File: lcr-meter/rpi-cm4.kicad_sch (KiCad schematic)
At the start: 0 parts

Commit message: Added CM4, basics of functionality started
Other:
- added sheet GPIO (CM4_GPIO.kicad_sch)
- added sheet High-Speed (CM4_HighSpeed.kicad_sch)
- added sheet RTC (RTC.kicad_sch)
- added sheet USB Hub (USB2-HUB.kicad_sch)
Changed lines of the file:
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@@
 	(generator_version "8.0")
 	(paper "A4")
+	(sheet
+		(at 66.04 124.46)
+		(size 43.18 33.02)
+		(fields_autoplaced yes)
+		(stroke
+			(width 0.1524)
+			(type solid)
+		)
+		(fill
+			(color 0 0 0 0.0000)
+		)
+		(property "Sheetname" "RTC"
+			(at 66.04 123.7484 0)
+			(effects
+				(font
+					(size 1.27 1.27)
+				)
+				(justify left bottom)
+			)
+		)
+		(property "Sheetfile" "RTC.kicad_sch"
+			(at 66.04 158.0646 0)
+			(effects
+				(font
+					(size 1.27 1.27)
+				)
+				(justify left top)
+			)
+		)
+		(instances
+			(project "lcr-meter"
+				(path "/ba333b18-b098-477b-9dd4-aab7b9764d9c/fa0205ff-d840-4c89-b6d9-0bee6ad4a2ef"
+					(page "10")
+				)
+			)
+		)
+	)
+	(sheet
+		(at 77.47 55.88)
+		(size 33.02 25.4)
+		(fields_autoplaced yes)
+		(stroke
+			(width 0.1524)
+			(type solid)
+		)
+		(fill
+			(color 0 0 0 0.0000)
+		)
+		(property "Sheetname" "GPIO"
+			(at 77.47 55.1684 0)
+			(effects
+				(font
+					(size 1.27 1.27)
+				)
+				(justify left bottom)
+			)
+		)
+		(property "Sheetfile" "CM4_GPIO.kicad_sch"
+			(at 77.47 81.8646 0)
+			(effects
+				(font
+					(size 1.27 1.27)
+				)
+				(justify left top)
+			)
+		)
+		(instances
+			(project "lcr-meter"
+				(path "/ba333b18-b098-477b-9dd4-aab7b9764d9c/fa0205ff-d840-4c89-b6d9-0bee6ad4a2ef"
+					(page "9")
+				)
+			)
+		)
+	)
+	(sheet
+		(at 205.74 76.2)
+		(size 30.48 20.32)
+		(fields_autoplaced yes)
+		(stroke
+			(width 0.1524)
+			(type solid)
+		)
+		(fill
+			(color 0 0 0 0.0000)
+		)
+		(property "Sheetname" "USB Hub"
+			(at 205.74 75.4884 0)
+			(effects
+				(font
+					(size 1.27 1.27)
+				)
+				(justify left bottom)
+			)
+		)
+		(property "Sheetfile" "USB2-HUB.kicad_sch"
+			(at 205.74 97.1046 0)
+			(effects
+				(font
+					(size 1.27 1.27)
+				)
+				(justify left top)
+			)
+		)
+		(instances
+			(project "lcr-meter"
+				(path "/ba333b18-b098-477b-9dd4-aab7b9764d9c/fa0205ff-d840-4c89-b6d9-0bee6ad4a2ef"
+					(page "11")
+				)
+			)
+		)
+	)
+	(sheet
+		(at 132.08 55.88)
+		(size 40.64 66.04)
+		(fields_autoplaced yes)
+		(stroke
+			(width 0.1524)
+			(type solid)
+		)
+		(fill
+			(color 0 0 0 0.0000)
+		)
+		(property "Sheetname" "High-Speed"
+			(at 132.08 55.1684 0)
+			(effects
+				(font
+					(size 1.27 1.27)
+				)
+				(justify left bottom)
+			)
+		)
+		(property "Sheetfile" "CM4_HighSpeed.kicad_sch"
+			(at 132.08 122.5046 0)
+			(effects
+				(font
+					(size 1.27 1.27)
+				)
+				(justify left top)
+			)
+		)
+		(instances
+			(project "lcr-meter"
+				(path "/ba333b18-b098-477b-9dd4-aab7b9764d9c/fa0205ff-d840-4c89-b6d9-0bee6ad4a2ef"
+					(page "8")
+				)
+			)
+		)
+	)
 )

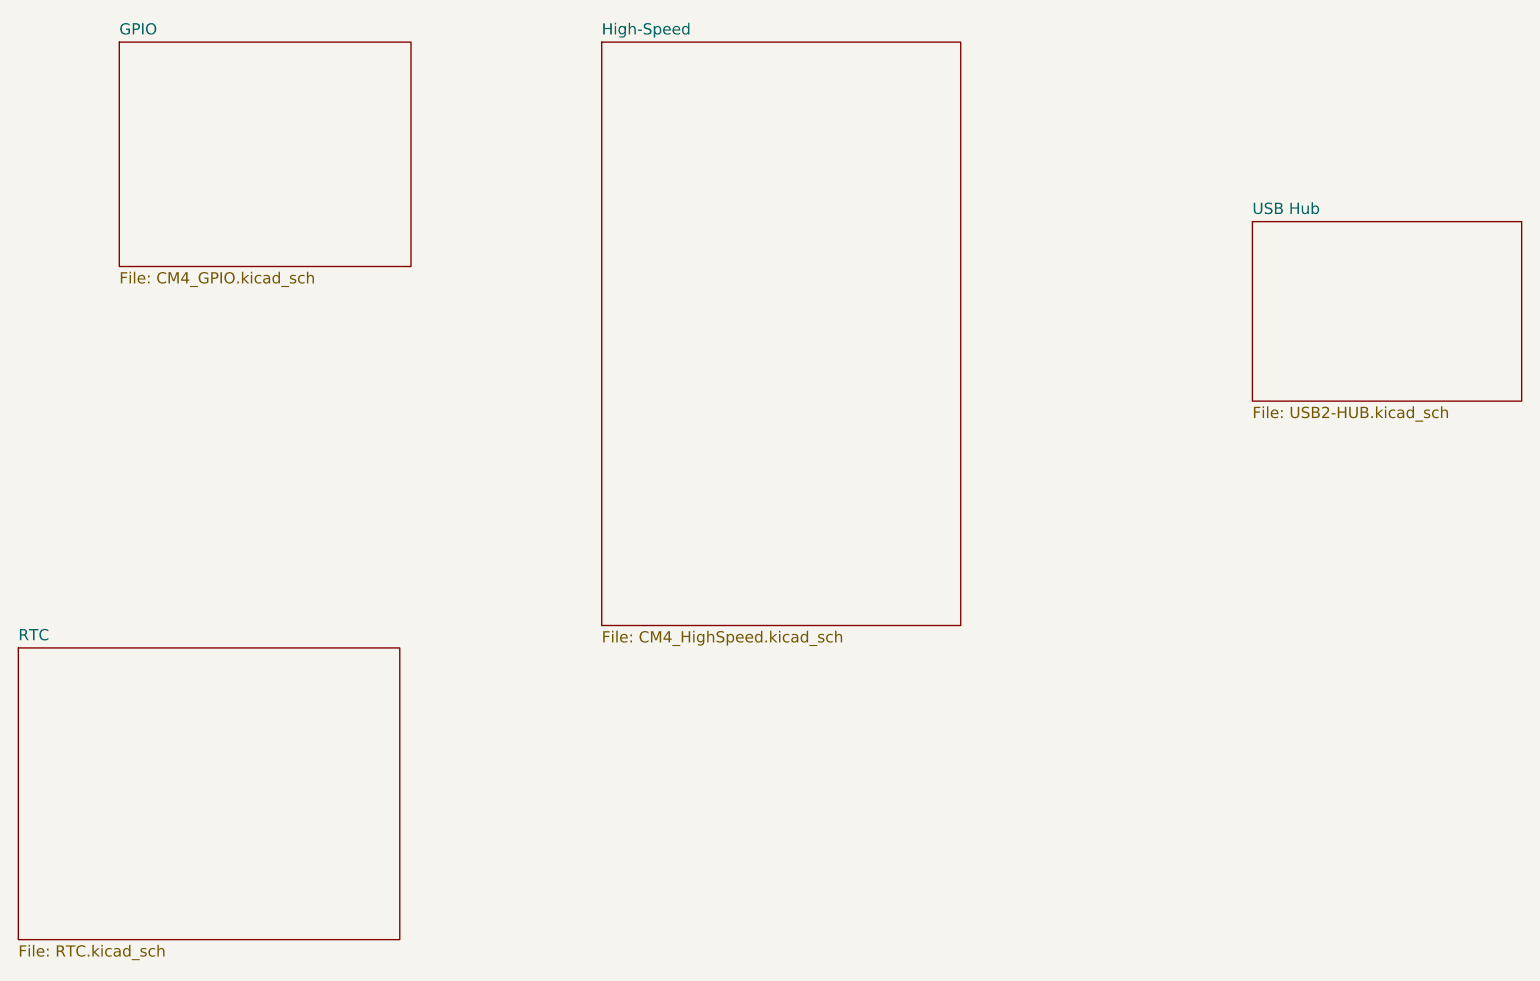
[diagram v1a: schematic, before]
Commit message: Progress, removal of unnecessary components
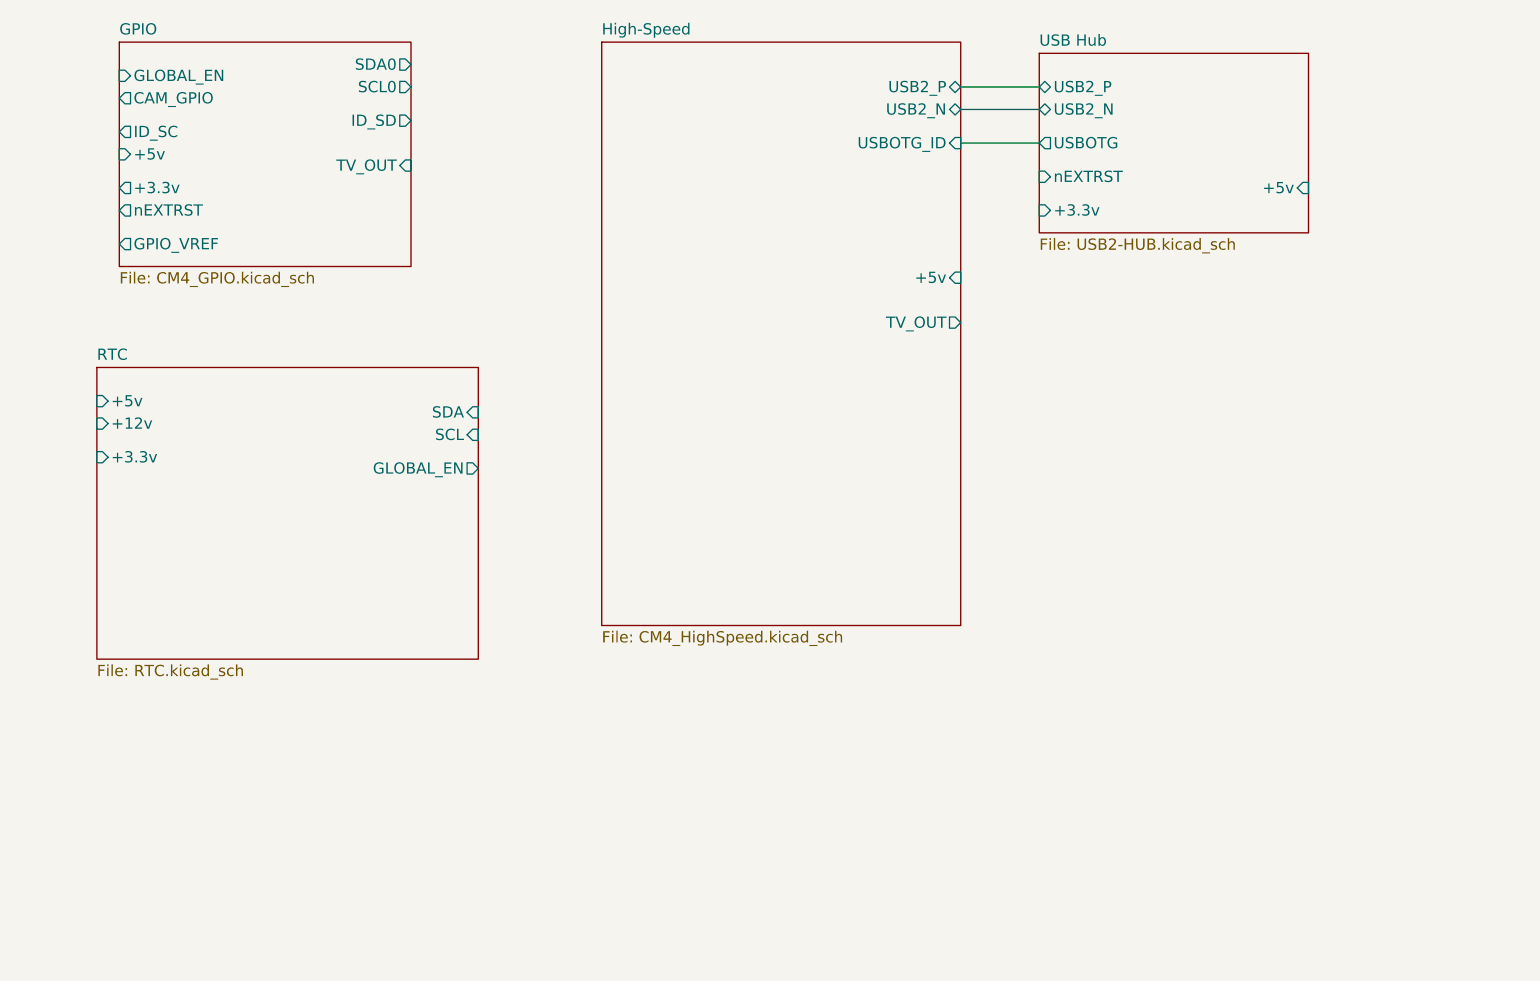
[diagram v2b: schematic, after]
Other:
- sheet GPIO ports: added +3.3v, +5v, CAM_GPIO, GLOBAL_EN, GPIO_VREF, ID_SC, ID_SD, SCL0, SDA0, TV_OUT, nEXTRST; removed none
- sheet High-Speed ports: added +5v, TV_OUT, USB2_N, USB2_P, USBOTG_ID; removed none
- sheet RTC ports: added +12v, +3.3v, +5v, GLOBAL_EN, SCL, SDA; removed none
- sheet USB Hub ports: added +3.3v, +5v, USB2_N, USB2_P, USBOTG, nEXTRST; removed none
